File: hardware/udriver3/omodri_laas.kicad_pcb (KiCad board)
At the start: 2 copper layers, 50 x 50 mm, 257 parts, among them J1 Conn_01x11, J10 Conn_01x07, J11 Conn_01x03, J12 Conn_01x03, J13 Conn_01x02, J2 Conn_01x05, J3 Conn_01x03, J4 Conn_01x03, J5 Conn_01x05, J6 Conn_01x05, J7 Conn_01x02, J8 Conn_01x07, J9 Conn_02x04_Odd_Even, Q1 CSD88599Q5DC, Q2 CSD88599Q5DC, Q3 CSD88599Q5DC, Q4 CSD88599Q5DC, Q5 CSD88599Q5DC, Q6 CSD88599Q5DC, SW1 B3U-3100P, U1 TMS320F28388D, U10 DSLVDS1048, U11 TPS3703, U12 TPS3703, U13 TPD6E05U06, U14 DSLVDS1047, U15 TPD2E001, U16 TPD2E001, U17 TPD2E001, U18 TPD2E001, U19 DRV8353S, U2 MAX17502FxTB, U20 DRV8353S, U3 MPM3804GG, U4 MPM3804GG, U5 REF6230, U6 OPA388, U7 TXB0106, U8 TCAN332G, U9 TPD6E05U06, X1 ECS-TXO-2016-33-200-TR

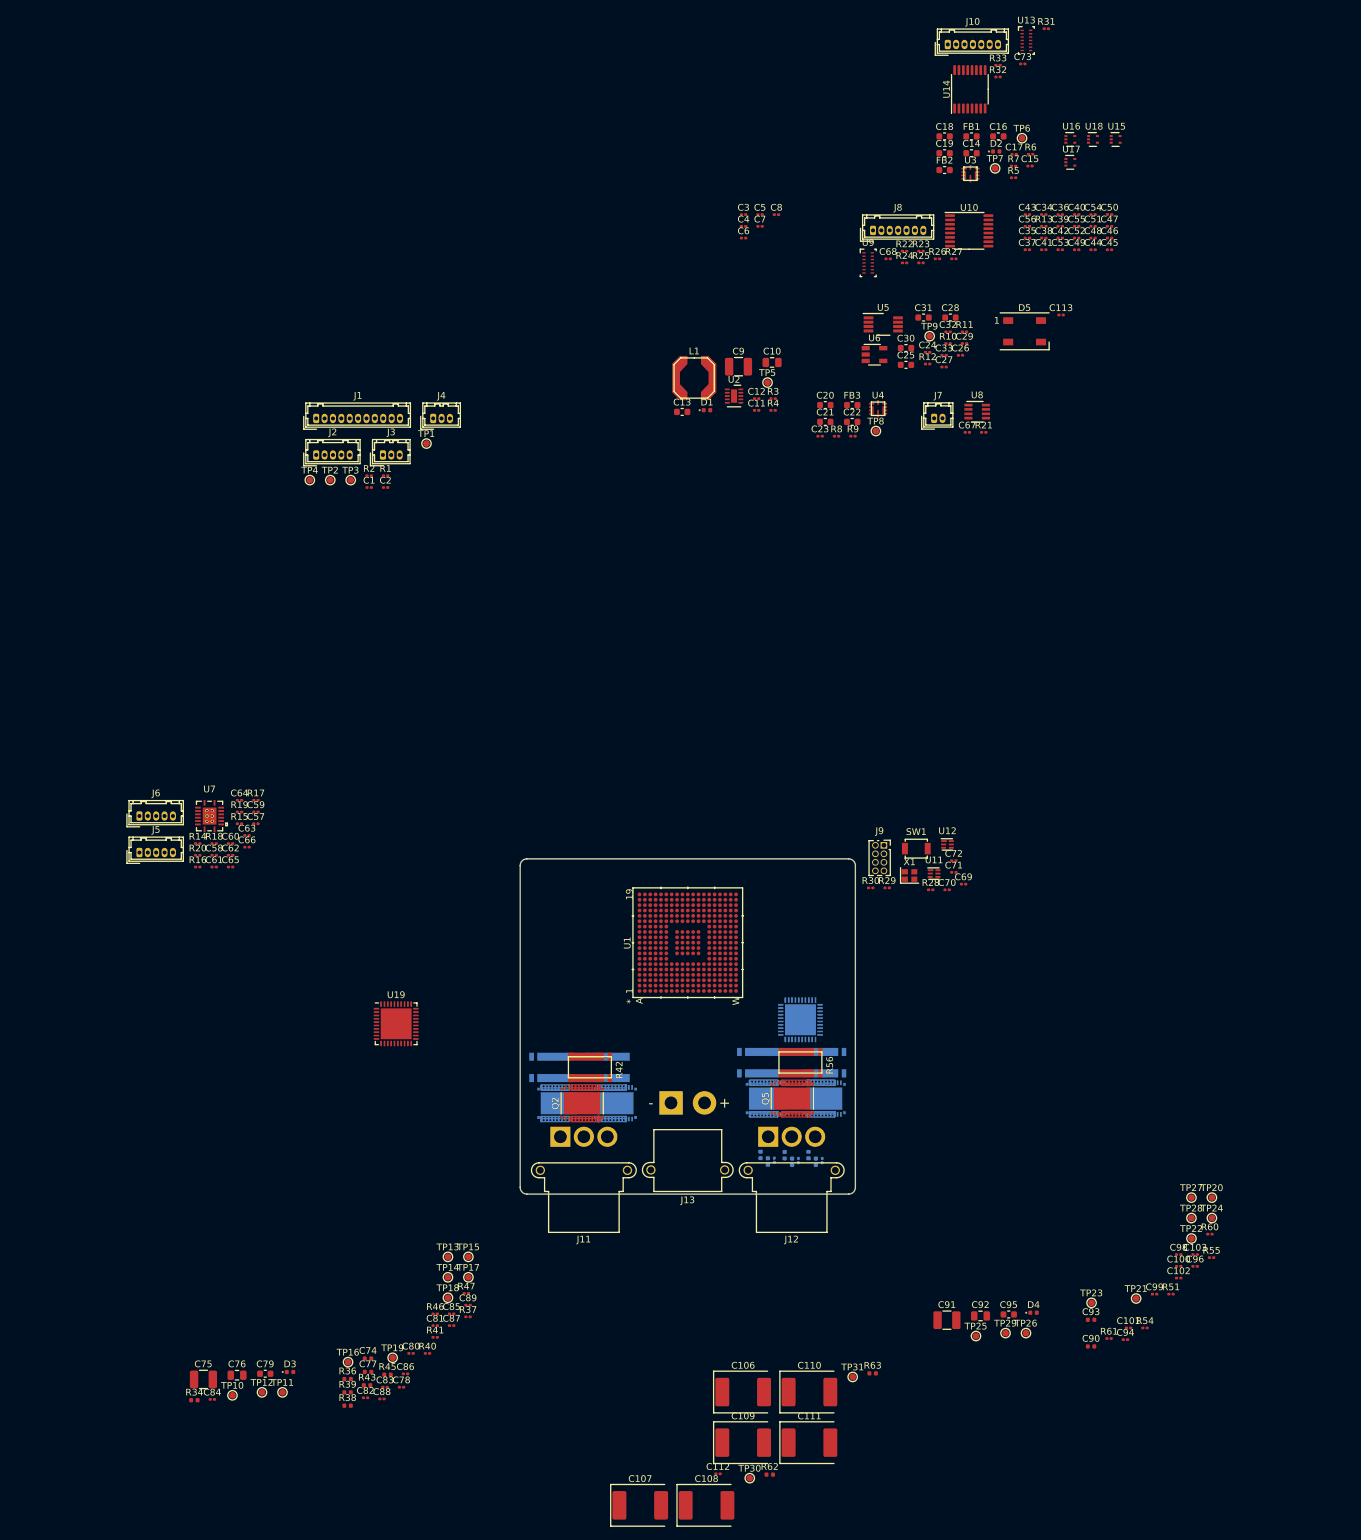
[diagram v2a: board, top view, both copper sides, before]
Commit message: Update of the schematics. Switches on GPIO72 & GPIO84 are missing. J1, J2 & J14 must be merged and connector placement optimized. TCXO must be changed from 20MHz to 25MHz for EtherCAT compatibility. PCB is partially routed in 6-Layers (mainly power supplies and and transistors). 8-Layers will be necessary.
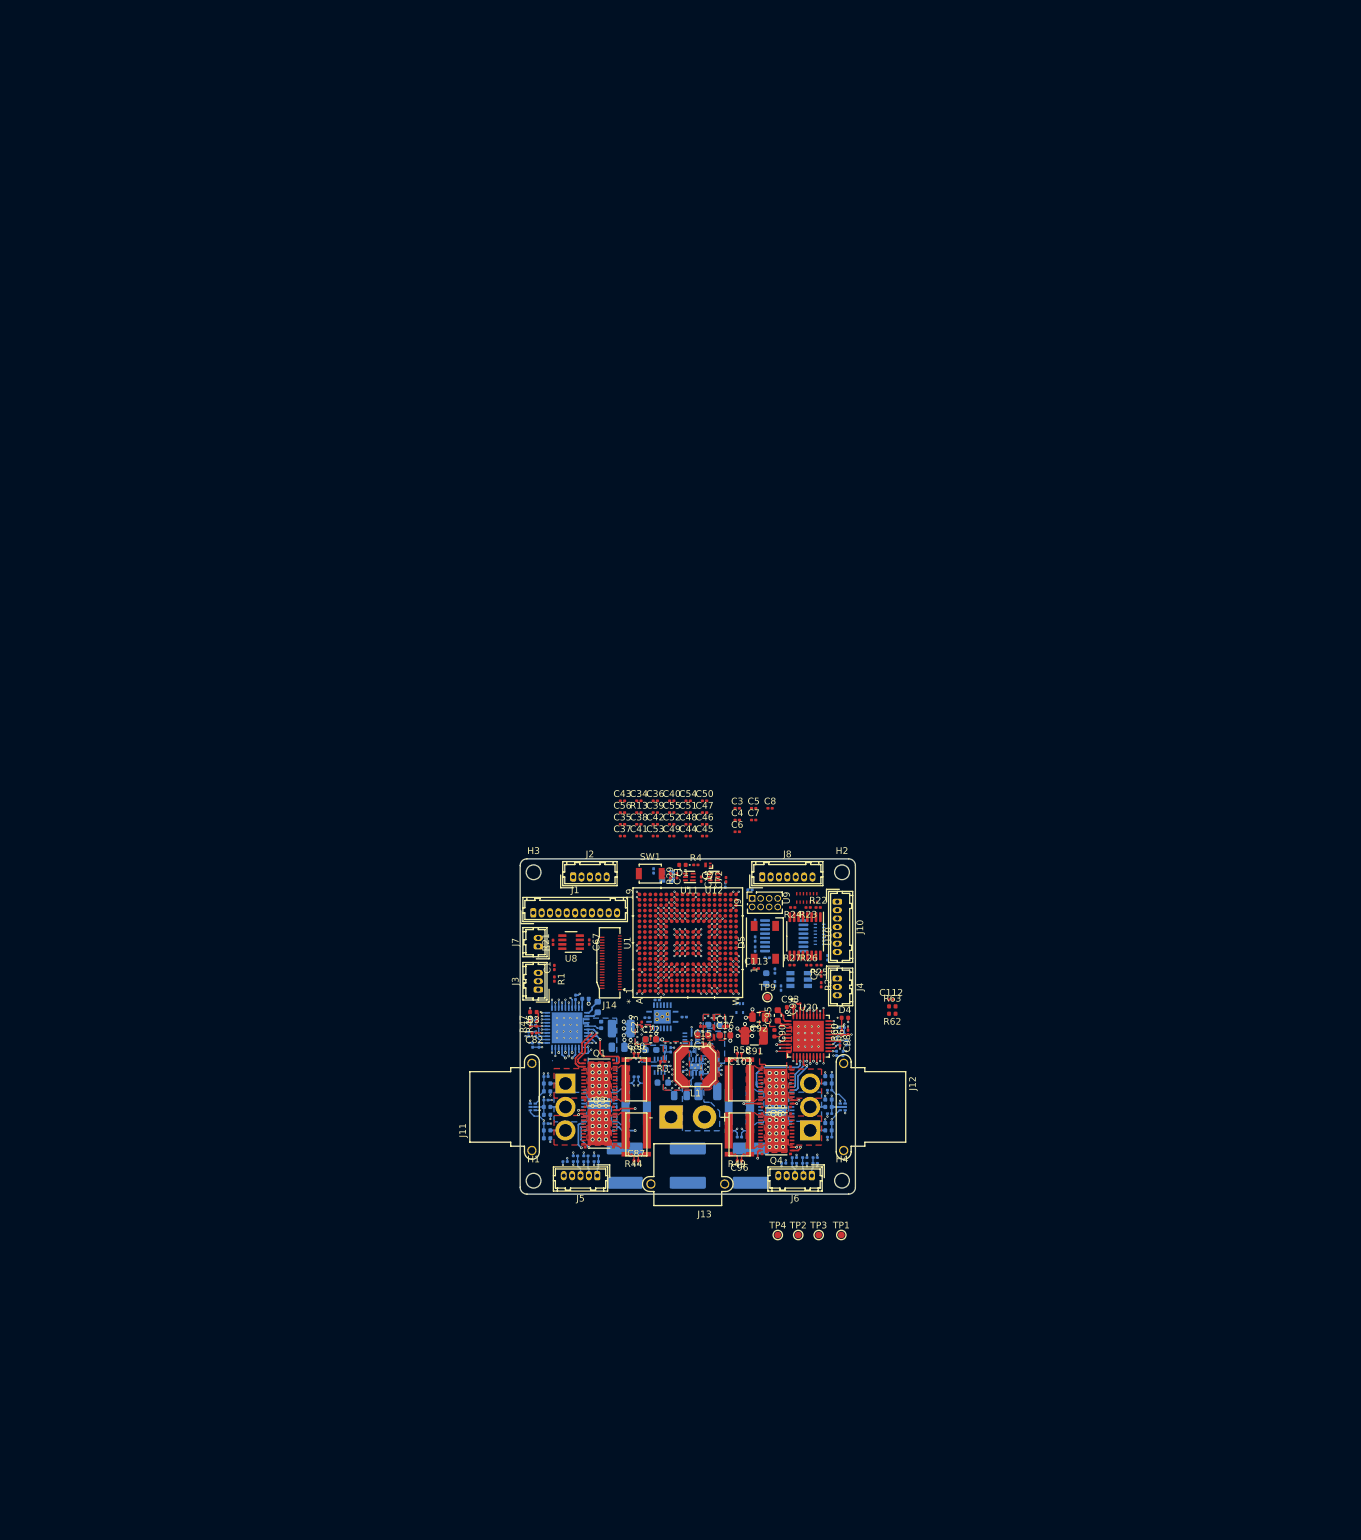
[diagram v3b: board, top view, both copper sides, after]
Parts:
- removed C106, C107, C108, C109, C110, C111: 100uF, Capacitor_Tantalum_SMD:CP_EIA-7360-38_Kemet-E
- removed C20, C25, C30, C31: 10uF, Capacitor_SMD:C_0603_1608Metric
- removed C24, C32, C33, C70: 100nF, Capacitor_SMD:C_0201_0603Metric
- removed D2: LED GREEN, LED_SMD:LED_0402_1005Metric
- removed R10, R11, R12: 0.1, Resistor_SMD:R_0201_0603Metric
- removed R7: 470, Resistor_SMD:R_0201_0603Metric
- removed TP10, TP11, TP12, TP13, TP14, TP15, TP16, TP17, TP18, TP19, TP20, TP21, TP22, TP23, TP24, TP25, TP26, TP27, TP28, TP29, TP30, TP31, TP5, TP6, TP7, TP8: TestPoint, TestPoint:TestPoint_Pad_D1.0mm
- removed U17, U18: TPD2E001, Package_SO:Texas_R-PDSO-N5
- added C114: 22uF, Capacitor_SMD:C_2220_5650Metric, B.Cu at (115.6, 95.8)
- added C115: 22uF, Capacitor_SMD:C_2220_5650Metric, B.Cu at (125.0, 95.8)
- added C116: 22uF, Capacitor_SMD:C_2220_5650Metric, B.Cu at (134.4, 95.8)
- added H1: MountingHole, MountingHole:MountingHole_2.2mm_M2, F.Cu at (102.0, 98.0)
- added H2: MountingHole, MountingHole:MountingHole_2.2mm_M2, F.Cu at (148.0, 52.0)
- added H3: MountingHole, MountingHole:MountingHole_2.2mm_M2, F.Cu at (102.0, 52.0)
- added H4: MountingHole, MountingHole:MountingHole_2.2mm_M2, F.Cu at (148.0, 98.0)
- added J14: Conn_01x40, Connector_FFC-FPC:JAE_FF0841SA1_2Rows-41Pins_P0.40mm_Horizontal, F.Cu at (113.5, 65.5)
- added Q7: NX7002BKM, Package_DFN_QFN:Diodes_DFN1006-3, F.Cu at (128.0, 50.9)
- C10, C100, C101, C102, C11, C12, C13, C26, C27, C28, C29, C57, C58, C59, C60, C61, C62, C63, C64, C65, C66, C68, C69, C73, C74, C75, C76, C77, C78, C79, C81, C83, C84, C85, C86, C88, C89, C9, C99, FB1, FB2, FB3, Q2, Q5, R14, R15, R16, R17, R18, R19, R20, R28, R30, R31, R32, R33, R34, R36, R37, R38, R39, R40, R41, R42, R43, R45, R5, R51, R54, R55, R56, R6, R8, R9, U13, U14, U15, U19, U2, U3, U4, U7, X1: moved to B.Cu
- C18: value 10uF -> 100nF; footprint Capacitor_SMD:C_0603_1608Metric -> Capacitor_SMD:C_0201_0603Metric
- C19, C21: value 22uF -> 10uF; moved to B.Cu
- J11, J12: footprint Connector_AMASS:AMASS_MR30PW-FB_1x03_P3.50mm_Horizontal -> udriver3:AMASS_MR30PW-FB_1x03_P3.50mm_Horizontal
- J13: footprint Connector_AMASS:AMASS_XT30PW-M_1x02_P2.50mm_Horizontal -> udriver3:AMASS_XT30PW-M_1x02_P2.50mm_Horizontal
- Q1, Q3, Q4, Q6, R35, R44, R49, R58, U20: moved to F.Cu
- R4: value 1k -> 470
- U16: value TPD2E001 -> TPD3E001; footprint Package_SO:Texas_R-PDSO-N5 -> udriver3:USON_6; moved to B.Cu
- U5: value REF6230 -> LT6654AIS6-3; footprint Package_SO:VSSOP-8_3.0x3.0mm_P0.65mm -> Package_TO_SOT_SMD:TSOT-23-6; moved to B.Cu
- U6: value OPA388 -> TPD3E001; footprint Package_TO_SOT_SMD:TSOT-23-5 -> udriver3:USON_6; moved to B.Cu
- moved U16 165.1 mm to (101.9, 87.0)
- moved R31 144.0 mm to (135.1, 63.5), turned to 90 degrees
- moved R6 141.7 mm to (127.7, 78.0), turned to 270 degrees
- moved U15 141.2 mm to (132.8, 72.2), turned to 270 degrees
- moved C19 140.2 mm to (129.3, 80.7), turned to 270 degrees
- moved C16 140.2 mm to (130.6, 76.3)
- moved FB1 138.9 mm to (128.1, 75.5), turned to 270 degrees
- moved C73 138.7 mm to (136.8, 64.8)
- moved C14 137.5 mm to (127.2, 76.3), turned to 180 degrees
- moved C15 137.3 mm to (127.2, 75.0), turned to 180 degrees
- moved R5 137.2 mm to (128.6, 78.0), turned to 90 degrees
- moved C17 137.0 mm to (130.6, 75.0)
- moved U13 136.8 mm to (144.7, 61.2)
- moved U3 135.5 mm to (125.6, 76.7)
- moved R32 133.6 mm to (135.1, 62.0), turned to 270 degrees
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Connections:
- net /Power distribution/Sheet5F5BD907/PG_5V0 renamed /Power distribution/OMODRI_Alim_1V2/PG_5V0
- net /Power distribution/Sheet5F5BE68A/3V3 renamed /Power distribution/OMODRI_Alim_3V3/3V3
- net /Power distribution/Sheet5F5BE68A/FB_3V3 renamed /Power distribution/OMODRI_Alim_3V3/FB_3V3
- net /Power distribution/Sheet5F5BF411/1V2 renamed /Power distribution/OMODRI_Alim_1V2/1V2
- net /Power distribution/Sheet5F5BF411/FB_1V2 renamed /Power distribution/OMODRI_Alim_1V2/FB_1V2
- net /Sheet5F71C5AE/DVDD renamed /OMODRI_driver_M1/DVDD
- net /Sheet5F71C5AE/GHA renamed /OMODRI_driver_M1/GHA
- net /Sheet5F71C5AE/GHB renamed /OMODRI_driver_M1/GHB
- net /Sheet5F71C5AE/GHC renamed /OMODRI_driver_M1/GHC
- net /Sheet5F71C5AE/GLA renamed /OMODRI_driver_M1/GLA
- net /Sheet5F71C5AE/GLB renamed /OMODRI_driver_M1/GLB
- net /Sheet5F71C5AE/GLC renamed /OMODRI_driver_M1/GLC
- net /Sheet5F71C5AE/INHA renamed /OMODRI_driver_M1/INHA
- net /Sheet5F71C5AE/INHB renamed /OMODRI_driver_M1/INHB
- net /Sheet5F71C5AE/INHC renamed /OMODRI_driver_M1/INHC
- net /Sheet5F71C5AE/INLA renamed /OMODRI_driver_M1/INLA
- net /Sheet5F71C5AE/INLB renamed /OMODRI_driver_M1/INLB
- net /Sheet5F71C5AE/INLC renamed /OMODRI_driver_M1/INLC
- net /Sheet5F71C5AE/MOTOR_CH1 renamed /OMODRI_driver_M1/MOTOR_CH1
- net /Sheet5F71C5AE/MOTOR_CH2 renamed /OMODRI_driver_M1/MOTOR_CH2
- net /Sheet5F71C5AE/MOTOR_CH3 renamed /OMODRI_driver_M1/MOTOR_CH3
- net /Sheet5F71C5AE/SHA renamed /OMODRI_driver_M1/SHA
- net /Sheet5F71C5AE/SHB renamed /OMODRI_driver_M1/SHB
- net /Sheet5F71C5AE/SHC renamed /OMODRI_driver_M1/SHC
- net /Sheet5F71C5AE/SNB renamed /OMODRI_driver_M1/SNB
- net /Sheet5F71C5AE/SNC renamed /OMODRI_driver_M1/SNC
- net /Sheet5F71C5AE/SPB renamed /OMODRI_driver_M1/SPB
- net /Sheet5F71C5AE/SPC renamed /OMODRI_driver_M1/SPC
- net /Sheet5F71C5AE/VGLS renamed /OMODRI_driver_M1/VGLS
- net /Sheet5F71C92D/DVDD renamed /OMODRI_driver_M2/DVDD
- net /Sheet5F71C92D/GHB renamed /OMODRI_driver_M2/GHB
- net /Sheet5F71C92D/GLB renamed /OMODRI_driver_M2/GLB
- net /Sheet5F71C92D/INHA renamed /OMODRI_driver_M2/INHA
- net /Sheet5F71C92D/INHB renamed /OMODRI_driver_M2/INHB
- net /Sheet5F71C92D/INHC renamed /OMODRI_driver_M2/INHC
- net /Sheet5F71C92D/INLA renamed /OMODRI_driver_M2/INLA
- net /Sheet5F71C92D/INLB renamed /OMODRI_driver_M2/INLB
- net /Sheet5F71C92D/INLC renamed /OMODRI_driver_M2/INLC
- net /Sheet5F71C92D/MOTOR_CH1 renamed /OMODRI_driver_M2/MOTOR_CH1
- net /Sheet5F71C92D/MOTOR_CH2 renamed /OMODRI_driver_M2/MOTOR_CH2
- net /Sheet5F71C92D/MOTOR_CH3 renamed /OMODRI_driver_M2/MOTOR_CH3
- net /Sheet5F71C92D/SHB renamed /OMODRI_driver_M2/SHB
- net /Sheet5F71C92D/SNB renamed /OMODRI_driver_M2/SNB
- net /Sheet5F71C92D/SPB renamed /OMODRI_driver_M2/SPB
- net /Sheet5F71C92D/VGLS renamed /OMODRI_driver_M2/VGLS
- net /Sheet5F9FCB8B/WS2812B_CMD renamed /OMODRI_GPIO/WS2812B_CMD
- net /sheet5F597565/ANALOG_IN1 renamed /OMODRI_GPIO/ANALOG_IN1
- net /sheet5F597565/ANALOG_IN2 renamed /OMODRI_GPIO/ANALOG_IN2
- net /sheet5F597565/COM_SPI_SIMO renamed /OMODRI_GPIO/COM_SPI_SIMO
- net /sheet5F597565/DRV1_GPIO_EN renamed /OMODRI_GPIO/DRV1_GPIO_EN
- net /sheet5F597565/DRV2_GPIO_EN renamed /OMODRI_GPIO/DRV2_GPIO_EN
- net /sheet5F597565/DRV_SPI_CLK renamed /OMODRI_GPIO/DRV_SPI_CLK
- net /sheet5F597565/DRV_SPI_SIMO renamed /OMODRI_GPIO/DRV_SPI_SIMO
- net /sheet5F597565/DRV_SPI_SOMI renamed /OMODRI_GPIO/DRV_SPI_SOMI
- net /sheet5F597565/ENC1_CHA renamed /OMODRI_GPIO/ENC1_CHA
- net /sheet5F597565/ENC1_CHB renamed /OMODRI_GPIO/ENC1_CHB
- net /sheet5F597565/ENC1_CHI renamed /OMODRI_GPIO/ENC1_CHI
- net /sheet5F597565/ENC2_CHB renamed /OMODRI_GPIO/ENC2_CHB
- net /sheet5F597565/FSI_TXA_D0 renamed /OMODRI_GPIO/FSI_TXA_D0
- net /sheet5F597565/FSI_TXA_D1 renamed /OMODRI_GPIO/FSI_TXA_D1
- net /sheet5F597565/GPIO2 renamed /OMODRI_GPIO/GPIO2
- net /sheet5F597565/M1_Ia renamed /OMODRI_GPIO/M1_Ia
- net /sheet5F597565/M1_Ib renamed /OMODRI_GPIO/M1_Ib
- net /sheet5F597565/M1_Ic renamed /OMODRI_GPIO/M1_Ic
- net /sheet5F597565/M1_Vbus renamed /OMODRI_GPIO/M1_Vbus
- net /sheet5F597565/M2_Ia renamed /OMODRI_GPIO/M2_Ia
- net /sheet5F597565/M2_Ib renamed /OMODRI_GPIO/M2_Ib
- net /sheet5F597565/M2_Ic renamed /OMODRI_GPIO/M2_Ic
- net /sheet5F597565/SPI_SIMO renamed /OMODRI_GPIO/SPI_SIMO
- net /sheet5F597565/~DRV1_GPIO_CSn~ renamed /OMODRI_GPIO/~DRV1_GPIO_CSn~
- net /sheet5F597565/~DRV1_GPIO_FAULTn~ renamed /OMODRI_GPIO/~DRV1_GPIO_FAULTn~
- net /sheet5F597565/~DRV2_GPIO_CSn~ renamed /OMODRI_GPIO/~DRV2_GPIO_CSn~
- net /sheet5F597565/~DRV2_GPIO_FAULTn~ renamed /OMODRI_GPIO/~DRV2_GPIO_FAULTn~
- net /sheet5F5A100E/ENC1_A renamed /OMODRI_QuadEncod/ENC1_A
- net /sheet5F5A100E/ENC1_B renamed /OMODRI_QuadEncod/ENC1_B
- net /sheet5F5A100E/ENC1_I renamed /OMODRI_QuadEncod/ENC1_I
- net /sheet5F5A100E/ENC2_B renamed /OMODRI_QuadEncod/ENC2_B
- net /sheet5F5B5755/CAN_H renamed /OMODRI_CAN/CAN_H
- net /sheet5F5B5755/CAN_L renamed /OMODRI_CAN/CAN_L
- net /sheet5F5DA2E4/TX_D0_LVDS_N renamed /OMODRI_FSI_TX/TX_D0_LVDS_N
- net /sheet5F5DA2E4/TX_D0_LVDS_P renamed /OMODRI_FSI_TX/TX_D0_LVDS_P
- C103 pad 1: /Sheet5F71C92D/SPC -> /OMODRI_driver_M2/SPC
- C103 pad 2: /Sheet5F71C92D/SNC -> /OMODRI_driver_M2/SNC
- C104 pad 1: /sheet5F597565/M2_Vb -> /OMODRI_GPIO/M2_Vb
- C105 pad 1: /sheet5F597565/M2_Vc -> /OMODRI_GPIO/M2_Vc
- C18 pad 1: 5V0 -> VDD_3V3
- C27 pad 1: Net-(C27-Pad1) -> VDDA_3V3
- C28 pad 1: Net-(C28-Pad1) -> REF_3V0_BUF
- C29 pad 1: /Power distribution/Sheet5F5C0182/REF_3V0 -> REF_3V0_BUF
- C63 pad 1: /sheet5F5A100E/ENC2_A -> /OMODRI_QuadEncod/ENC2_A
- C65 pad 1: /sheet5F5A100E/ENC2_I -> /OMODRI_QuadEncod/ENC2_I
- C80 pad 1: /Sheet5F71C5AE/SPA -> /OMODRI_driver_M1/SPA
- C80 pad 2: /Sheet5F71C5AE/SNA -> /OMODRI_driver_M1/SNA
- C81 pad 1: /sheet5F597565/M1_Va -> /OMODRI_GPIO/M1_Va
- C88 pad 1: /sheet5F597565/M1_Vb -> /OMODRI_GPIO/M1_Vb
- C89 pad 1: /sheet5F597565/M1_Vc -> /OMODRI_GPIO/M1_Vc
- C96 pad 1: /Sheet5F71C92D/SPA -> /OMODRI_driver_M2/SPA
- C96 pad 2: /Sheet5F71C92D/SNA -> /OMODRI_driver_M2/SNA
- C97 pad 1: /sheet5F597565/M2_Va -> /OMODRI_GPIO/M2_Va
- D1 pad 2: 5V0 -> VDD_3V3
- J1 pad 10: /sheet5F597565/GPIO3 -> /OMODRI_GPIO/GPIO1
- J1 pad 11: /sheet5F597565/GPIO4 -> /OMODRI_GPIO/GPIO0
- J1 pad 3: /sheet5F597565/COM_SPI_SOMI -> /OMODRI_GPIO/~COM_SPI_CSn~
- J1 pad 4: /sheet5F597565/COM_SPI_CLK -> /OMODRI_GPIO/COM_SPI_SOMI
- J1 pad 5: /sheet5F597565/~COM_SPI_CSn~ -> /OMODRI_GPIO/COM_SPI_CLK
- J1 pad 7: /sheet5F597565/GPIO0 -> /OMODRI_GPIO/GPIO4
- J1 pad 8: /sheet5F597565/GPIO1 -> /OMODRI_GPIO/GPIO3
- J10 pad 2: /sheet5F5DA2E4/TX_CLK_LVDS_N -> /OMODRI_FSI_TX/TX_CLK_LVDS_N
- J10 pad 3: /sheet5F5DA2E4/TX_CLK_LVDS_P -> /OMODRI_FSI_TX/TX_CLK_LVDS_P
- J10 pad 6: /sheet5F5DA2E4/TX_D1_LVDS_N -> /OMODRI_FSI_TX/TX_D1_LVDS_P
- J10 pad 7: /sheet5F5DA2E4/TX_D1_LVDS_P -> /OMODRI_FSI_TX/TX_D1_LVDS_N
- J13 pad 1: VPOWER -> GND
- J13 pad 2: GND -> VPOWER
- J2 pad 2: /sheet5F597565/SPI_SOMI -> /OMODRI_GPIO/~SPI_CSn~
- J2 pad 3: /sheet5F597565/SPI_CLK -> /OMODRI_GPIO/SPI_SOMI
- J2 pad 4: /sheet5F597565/~SPI_CSn~ -> /OMODRI_GPIO/SPI_CLK
- J6 pad 1: /sheet5F5A100E/ENC2_A -> /OMODRI_QuadEncod/ENC2_A
- J6 pad 3: /sheet5F5A100E/ENC2_I -> /OMODRI_QuadEncod/ENC2_I
- J8 pad 2: /sheet5F5B5756/RX_CLK_LVDS_N -> /OMODRI_FSI_RX/RX_CLK_LVDS_N
- J8 pad 3: /sheet5F5B5756/RX_CLK_LVDS_P -> /OMODRI_FSI_RX/RX_CLK_LVDS_P
- J8 pad 4: /sheet5F5B5756/RX_D0_LVDS_N -> /OMODRI_FSI_RX/RX_D0_LVDS_N
- J8 pad 5: /sheet5F5B5756/RX_D0_LVDS_P -> /OMODRI_FSI_RX/RX_D0_LVDS_P
- J8 pad 6: /sheet5F5B5756/RX_D1_LVDS_N -> /OMODRI_FSI_RX/RX_D1_LVDS_P
- J8 pad 7: /sheet5F5B5756/RX_D1_LVDS_P -> /OMODRI_FSI_RX/RX_D1_LVDS_N
- Q4 pad 1: /Sheet5F71C92D/GHA -> /OMODRI_driver_M2/GHA
- Q4 pad 2: /Sheet5F71C92D/SHA -> /OMODRI_driver_M2/SHA
- Q4 pad 22: /Sheet5F71C92D/GLA -> /OMODRI_driver_M2/GLA
- Q6 pad 1: /Sheet5F71C92D/GHC -> /OMODRI_driver_M2/GHC
- Q6 pad 2: /Sheet5F71C92D/SHC -> /OMODRI_driver_M2/SHC
- Q6 pad 22: /Sheet5F71C92D/GLC -> /OMODRI_driver_M2/GLC
- R17 pad 2: /sheet5F5A100E/ENC2_A -> /OMODRI_QuadEncod/ENC2_A
- R19 pad 2: /sheet5F5A100E/ENC2_I -> /OMODRI_QuadEncod/ENC2_I
- R22 pad 1: /sheet5F5B5756/RX_CLK_LVDS_P -> /OMODRI_FSI_RX/RX_D1_LVDS_P
- R22 pad 2: /sheet5F5B5756/RX_CLK_LVDS_N -> /OMODRI_FSI_RX/RX_D1_LVDS_N
- R23 pad 1: /sheet5F5B5756/RX_D0_LVDS_P -> /OMODRI_FSI_RX/RX_D0_LVDS_P
- R23 pad 2: /sheet5F5B5756/RX_D0_LVDS_N -> /OMODRI_FSI_RX/RX_D0_LVDS_N
- R24 pad 1: /sheet5F5B5756/RX_D1_LVDS_P -> /OMODRI_FSI_RX/RX_CLK_LVDS_P
- R24 pad 2: /sheet5F5B5756/RX_D1_LVDS_N -> /OMODRI_FSI_RX/RX_CLK_LVDS_N
- R25 pad 2: /sheet5F597565/FSI_RXA_CLK -> /OMODRI_GPIO/FSI_RXC_D1
- R26 pad 2: /sheet5F597565/FSI_RXA_D0 -> /OMODRI_GPIO/FSI_RXC_D0
- R27 pad 2: /sheet5F597565/FSI_RXA_D1 -> /OMODRI_GPIO/FSI_RXC_CLK
- R33 pad 2: /sheet5F597565/FSI_TXA_CLK -> /OMODRI_GPIO/FSI_TXA_CLK
- R34 pad 2: /sheet5F597565/M1_Va -> /OMODRI_GPIO/M1_Va
- R35 pad 1: GND -> Net-(Q1-Pad12)
- R35 pad 2: /Sheet5F71C5AE/SNA -> /OMODRI_driver_M1/SPA
- R35 pad 3: /Sheet5F71C5AE/SPA -> /OMODRI_driver_M1/SNA
- R35 pad 4: Net-(Q1-Pad12) -> GND
- R36 pad 1: /sheet5F597565/M1_Va -> /OMODRI_GPIO/M1_Va
- R38 pad 2: /sheet5F597565/M1_Vb -> /OMODRI_GPIO/M1_Vb
- R39 pad 2: /sheet5F597565/M1_Vc -> /OMODRI_GPIO/M1_Vc
- R4 pad 2: GND -> Net-(Q7-Pad3)
- R43 pad 1: /sheet5F597565/M1_Vb -> /OMODRI_GPIO/M1_Vb
- R45 pad 1: /sheet5F597565/M1_Vc -> /OMODRI_GPIO/M1_Vc
- R48 pad 2: /sheet5F597565/M2_Va -> /OMODRI_GPIO/M2_Va
- R49 pad 1: GND -> Net-(Q4-Pad12)
- R49 pad 2: /Sheet5F71C92D/SNA -> /OMODRI_driver_M2/SPA
- R49 pad 3: /Sheet5F71C92D/SPA -> /OMODRI_driver_M2/SNA
- R49 pad 4: Net-(Q4-Pad12) -> GND
- R50 pad 1: /sheet5F597565/M2_Va -> /OMODRI_GPIO/M2_Va
- R52 pad 2: /sheet5F597565/M2_Vb -> /OMODRI_GPIO/M2_Vb
- R53 pad 2: /sheet5F597565/M2_Vc -> /OMODRI_GPIO/M2_Vc
- R57 pad 1: /sheet5F597565/M2_Vb -> /OMODRI_GPIO/M2_Vb
- R58 pad 1: Net-(Q6-Pad12) -> GND
- R58 pad 2: /Sheet5F71C92D/SPC -> /OMODRI_driver_M2/SNC
- R58 pad 3: /Sheet5F71C92D/SNC -> /OMODRI_driver_M2/SPC
- R58 pad 4: GND -> Net-(Q6-Pad12)
- R59 pad 1: /sheet5F597565/M2_Vc -> /OMODRI_GPIO/M2_Vc
- U1 pad A12: Net-(U1-PadA12) -> /OMODRI_GPIO/ESC_MDIO_DATA
- U1 pad A13: Net-(U1-PadA13) -> /OMODRI_GPIO/ESC_PHY1_LINKSTATUS
- U1 pad A14: /sheet5F597565/GPIO4 -> /OMODRI_GPIO/GPIO4
- U1 pad A16: /sheet5F597565/GPIO0 -> /OMODRI_GPIO/GPIO0
- U1 pad A17: /sheet5F597565/SPI_SOMI -> /OMODRI_GPIO/SPI_SOMI
- U1 pad A8: Net-(U1-PadA8) -> /OMODRI_GPIO/ESC_RX0_CLK
- U1 pad B10: Net-(U1-PadB10) -> /OMODRI_GPIO/ESC_TX0_CLK
- U1 pad B12: Net-(U1-PadB12) -> /OMODRI_GPIO/ECAT0_INT
- U1 pad B13: Net-(U1-PadB13) -> /OMODRI_GPIO/ESC_I2C_SDA
- U1 pad B14: /sheet5F597565/GPIO3 -> /OMODRI_GPIO/GPIO3
- U1 pad B15: /sheet5F597565/GPIO1 -> /OMODRI_GPIO/GPIO1
- U1 pad B16: /sheet5F597565/~SPI_CSn~ -> /OMODRI_GPIO/~SPI_CSn~
- U1 pad B17: /sheet5F597565/SPI_CLK -> /OMODRI_GPIO/SPI_CLK
- U1 pad B8: Net-(U1-PadB8) -> /OMODRI_GPIO/ESC_RX0_ERR
- U1 pad B9: Net-(U1-PadB9) -> /OMODRI_GPIO/ESC_TX0_D2
- U1 pad C10: Net-(U1-PadC10) -> /OMODRI_GPIO/ESC_TX0_D0
- U1 pad C12: Net-(U1-PadC12) -> /OMODRI_GPIO/~ESC_PHY_RESETn~
- U1 pad C13: Net-(U1-PadC13) -> /OMODRI_GPIO/ESC_I2C_SCL
- U1 pad C2: Net-(U1-PadC2) -> /OMODRI_GPIO/CAN_TX
- U1 pad C4: Net-(U1-PadC4) -> /OMODRI_GPIO/ESC_RX0_D2
- U1 pad C5: Net-(U1-PadC5) -> /OMODRI_GPIO/ESC_RX0_D0
- U1 pad C9: Net-(U1-PadC9) -> /OMODRI_GPIO/ESC_TX0_D3
- U1 pad D1: Net-(U1-PadD1) -> /OMODRI_GPIO/CAN_RX
- U1 pad D10: Net-(U1-PadD10) -> /OMODRI_GPIO/ESC_TX0_D1
- U1 pad D12: Net-(U1-PadD12) -> /OMODRI_GPIO/ESC_TX0_ENA
- U1 pad D13: Net-(U1-PadD13) -> /OMODRI_GPIO/ESC_MDIO_CLK
- U1 pad D14: Net-(U1-PadD14) -> /OMODRI_GPIO/ESC_PHY0_LINKSTATUS
- U1 pad D18: Net-(U1-PadD18) -> /OMODRI_GPIO/ESC_LED_RUN
- U1 pad D4: Net-(U1-PadD4) -> /OMODRI_GPIO/ESC_RX0_D3
- U1 pad D5: Net-(U1-PadD5) -> /OMODRI_GPIO/ESC_RX0_D1
- U1 pad D9: Net-(U1-PadD9) -> /OMODRI_GPIO/ESC_RX0_DV
- U1 pad E17: Net-(U1-PadE17) -> /OMODRI_GPIO/ESC_LED_ERR
- U1 pad F17: Net-(U1-PadF17) -> /OMODRI_GPIO/ESC_LED_LINK1_ACTIVE
- U1 pad F18: Net-(U1-PadF18) -> /OMODRI_GPIO/ESC_LED_LINK0_ACTIVE
- U1 pad J16: /sheet5F597565/CAN_TX -> Net-(U1-PadJ16)
- U1 pad J17: /sheet5F597565/CAN_RX -> Net-(U1-PadJ17)
- U1 pad K1: /sheet5F597565/ENC2_CHI -> /OMODRI_GPIO/ENC2_CHI
- U1 pad K16: /sheet5F597565/COM_SPI_CLK -> /OMODRI_GPIO/COM_SPI_CLK
- U1 pad K3: /sheet5F597565/ENC2_CHA -> /OMODRI_GPIO/ENC2_CHA
- U1 pad L16: /sheet5F597565/COM_SPI_SOMI -> /OMODRI_GPIO/COM_SPI_SOMI
- U1 pad L19: Net-(U1-PadL19) -> /OMODRI_GPIO/ESC_RX1_D3
- U1 pad M16: /sheet5F597565/~COM_SPI_CSn~ -> /OMODRI_GPIO/~COM_SPI_CSn~
- U1 pad M18: Net-(U1-PadM18) -> /OMODRI_GPIO/ESC_RX1_D2
- U1 pad M19: Net-(U1-PadM19) -> /OMODRI_GPIO/ESC_RX1_D1
- U1 pad N19: Net-(U1-PadN19) -> /OMODRI_GPIO/ESC_RX1_D0
- U1 pad P16: /sheet5F597565/FSI_RXA_D0 -> Net-(U1-PadP16)
- U1 pad P17: /sheet5F597565/FSI_RXA_D1 -> Net-(U1-PadP17)
- U1 pad P18: /sheet5F597565/FSI_RXA_CLK -> Net-(U1-PadP18)
- U1 pad R19: /sheet5F597565/FSI_TXA_CLK -> /OMODRI_GPIO/FSI_TXA_CLK
- U1 pad T10: Net-(U1-PadT10) -> /OMODRI_GPIO/ESC_TX1_ENA
- U1 pad T17: Net-(U1-PadT17) -> /OMODRI_GPIO/ESC_RX1_DV
- U1 pad T18: Net-(U1-PadT18) -> /OMODRI_GPIO/ESC_RX1_CLK
- U1 pad T19: Net-(U1-PadT19) -> /OMODRI_GPIO/ESC_RX1_ERR
- U1 pad T2: /sheet5F597565/M2_Va -> /OMODRI_GPIO/M2_Va
- U1 pad T6: /sheet5F597565/M1_Vc -> /OMODRI_GPIO/M1_Vc
- U1 pad U10: Net-(U1-PadU10) -> /OMODRI_GPIO/ESC_TX1_CLK
- U1 pad U12: Net-(U1-PadU12) -> /OMODRI_GPIO/FSI_RXC_CLK
- U1 pad U18: Net-(U1-PadU18) -> /OMODRI_GPIO/ESC_TX1_D3
- U1 pad U2: /sheet5F597565/M1_Va -> /OMODRI_GPIO/M1_Va
- U1 pad U6: /sheet5F597565/M2_Vc -> /OMODRI_GPIO/M2_Vc
- U1 pad V10: Net-(U1-PadV10) -> /OMODRI_GPIO/ESC_TX1_D0
- U1 pad V12: Net-(U1-PadV12) -> /OMODRI_GPIO/FSI_RXC_D0
- U1 pad V18: Net-(U1-PadV18) -> /OMODRI_GPIO/ESC_TX1_D2
- U1 pad V3: /sheet5F597565/M1_Vb -> /OMODRI_GPIO/M1_Vb
- U1 pad W10: Net-(U1-PadW10) -> /OMODRI_GPIO/FSI_RXC_D1
- U1 pad W18: Net-(U1-PadW18) -> /OMODRI_GPIO/ESC_TX1_D1
- U1 pad W3: /sheet5F597565/M2_Vb -> /OMODRI_GPIO/M2_Vb
- U1 pad W9: Net-(U1-PadW9) -> /OMODRI_GPIO/ECAT1_INT
- U10 pad 1: /sheet5F5B5756/RX_CLK_LVDS_N -> /OMODRI_FSI_RX/RX_D1_LVDS_N
- U10 pad 10: Net-(U10-Pad10) -> /OMODRI_GPIO/FSI_RXC_CLK
- U10 pad 11: /sheet5F597565/FSI_RXA_D1 -> Net-(U10-Pad11)
- U10 pad 14: /sheet5F597565/FSI_RXA_D0 -> /OMODRI_GPIO/FSI_RXC_D0
- U10 pad 15: /sheet5F597565/FSI_RXA_CLK -> /OMODRI_GPIO/FSI_RXC_D1
- U10 pad 2: /sheet5F5B5756/RX_CLK_LVDS_P -> /OMODRI_FSI_RX/RX_D1_LVDS_P
- U10 pad 3: /sheet5F5B5756/RX_D0_LVDS_P -> /OMODRI_FSI_RX/RX_D0_LVDS_P
- U10 pad 4: /sheet5F5B5756/RX_D0_LVDS_N -> /OMODRI_FSI_RX/RX_D0_LVDS_N
- U10 pad 5: /sheet5F5B5756/RX_D1_LVDS_N -> Net-(U10-Pad5)
- U10 pad 6: /sheet5F5B5756/RX_D1_LVDS_P -> Net-(U10-Pad6)
- U10 pad 7: Net-(U10-Pad7) -> /OMODRI_FSI_RX/RX_CLK_LVDS_P
- U10 pad 8: Net-(U10-Pad8) -> /OMODRI_FSI_RX/RX_CLK_LVDS_N
- U13 pad 1: /sheet5F5DA2E4/TX_CLK_LVDS_N -> /OMODRI_FSI_TX/TX_D1_LVDS_N
- U13 pad 13: /sheet5F5DA2E4/TX_CLK_LVDS_P -> /OMODRI_FSI_TX/TX_D1_LVDS_P
- U13 pad 14: /sheet5F5DA2E4/TX_CLK_LVDS_N -> /OMODRI_FSI_TX/TX_D1_LVDS_N
- U13 pad 2: /sheet5F5DA2E4/TX_CLK_LVDS_P -> /OMODRI_FSI_TX/TX_D1_LVDS_P
- U13 pad 6: /sheet5F5DA2E4/TX_D1_LVDS_N -> /OMODRI_FSI_TX/TX_CLK_LVDS_P
- U13 pad 7: /sheet5F5DA2E4/TX_D1_LVDS_P -> /OMODRI_FSI_TX/TX_CLK_LVDS_N
- U13 pad 8: /sheet5F5DA2E4/TX_D1_LVDS_P -> /OMODRI_FSI_TX/TX_CLK_LVDS_N
- U13 pad 9: /sheet5F5DA2E4/TX_D1_LVDS_N -> /OMODRI_FSI_TX/TX_CLK_LVDS_P
- U14 pad 10: Net-(U14-Pad10) -> /OMODRI_FSI_TX/TX_CLK_LVDS_P
- U14 pad 11: /sheet5F5DA2E4/TX_D1_LVDS_P -> Net-(U14-Pad11)
- U14 pad 12: /sheet5F5DA2E4/TX_D1_LVDS_N -> Net-(U14-Pad12)
- U14 pad 15: /sheet5F5DA2E4/TX_CLK_LVDS_P -> /OMODRI_FSI_TX/TX_D1_LVDS_P
- U14 pad 16: /sheet5F5DA2E4/TX_CLK_LVDS_N -> /OMODRI_FSI_TX/TX_D1_LVDS_N
- U14 pad 6: /sheet5F597565/FSI_TXA_CLK -> Net-(U14-Pad6)
- U14 pad 7: Net-(U14-Pad7) -> /OMODRI_GPIO/FSI_TXA_CLK
- U14 pad 9: Net-(U14-Pad9) -> /OMODRI_FSI_TX/TX_CLK_LVDS_N
- U15 pad 1: VDDA_3V3 -> VDD_3V3
- U16 pad 1: VDDA_3V3 -> /OMODRI_GPIO/M1_Vc
- U16 pad 2: /sheet5F597565/M2_Vb -> /OMODRI_GPIO/M1_Vb
- U16 pad 3: /sheet5F597565/M1_Vb -> GND
- U16 pad 4: GND -> /OMODRI_GPIO/M1_Va
- U16 pad 5: /sheet5F597565/M2_Vb -> /OMODRI_GPIO/M1_Vb
- U19 pad 10: /Sheet5F71C5AE/SNA -> /OMODRI_driver_M1/SNA
- U19 pad 9: /Sheet5F71C5AE/SPA -> /OMODRI_driver_M1/SPA
- U20 pad 10: /Sheet5F71C92D/SNC -> /OMODRI_driver_M2/SNA
- U20 pad 16: /Sheet5F71C92D/GHA -> /OMODRI_driver_M2/GHC
- U20 pad 17: /Sheet5F71C92D/SHA -> /OMODRI_driver_M2/SHC
- U20 pad 18: /Sheet5F71C92D/GLA -> /OMODRI_driver_M2/GLC
- U20 pad 19: /Sheet5F71C92D/SPA -> /OMODRI_driver_M2/SPC
- U20 pad 20: /Sheet5F71C92D/SNA -> /OMODRI_driver_M2/SNC
- U20 pad 6: /Sheet5F71C92D/GHC -> /OMODRI_driver_M2/GHA
- U20 pad 7: /Sheet5F71C92D/SHC -> /OMODRI_driver_M2/SHA
- U20 pad 8: /Sheet5F71C92D/GLC -> /OMODRI_driver_M2/GLA
- U20 pad 9: /Sheet5F71C92D/SPC -> /OMODRI_driver_M2/SPA
- U5 pad 1: VDDA_3V3 -> GND
- U5 pad 2: VDDA_3V3 -> GND
- U5 pad 3: VDDA_3V3 -> Net-(U5-Pad3)
- U5 pad 4: Net-(C27-Pad1) -> VDDA_3V3
- U5 pad 5: /Power distribution/Sheet5F5C0182/REF_3V0 -> Net-(U5-Pad5)
- U5 pad 6: /Power distribution/Sheet5F5C0182/REF_3V0 -> REF_3V0_BUF
- U6 pad 1: REF_3V0_BUF -> /OMODRI_GPIO/M2_Vc
- U6 pad 2: GND -> /OMODRI_GPIO/M2_Vb
- U6 pad 3: /Power distribution/Sheet5F5C0182/REF_3V0 -> GND
- U6 pad 4: REF_3V0_BUF -> /OMODRI_GPIO/M2_Va
- U6 pad 5: VDDA_3V3 -> /OMODRI_GPIO/M2_Vb
- U7 pad 10: /sheet5F5A100E/ENC2_I -> /OMODRI_QuadEncod/ENC2_A
- U7 pad 12: /sheet5F5A100E/ENC2_A -> /OMODRI_QuadEncod/ENC2_I
- U7 pad 5: /sheet5F597565/ENC2_CHA -> /OMODRI_GPIO/ENC2_CHI
- U7 pad 7: /sheet5F597565/ENC2_CHI -> /OMODRI_GPIO/ENC2_CHA
- U8 pad 1: /sheet5F597565/CAN_TX -> /OMODRI_GPIO/CAN_TX
- U8 pad 4: /sheet5F597565/CAN_RX -> /OMODRI_GPIO/CAN_RX
- U9 pad 1: /sheet5F5B5756/RX_CLK_LVDS_N -> /OMODRI_FSI_RX/RX_CLK_LVDS_N
- U9 pad 11: /sheet5F5B5756/RX_D0_LVDS_N -> /OMODRI_FSI_RX/RX_D0_LVDS_P
- U9 pad 12: /sheet5F5B5756/RX_D0_LVDS_P -> /OMODRI_FSI_RX/RX_D0_LVDS_N
- U9 pad 13: /sheet5F5B5756/RX_CLK_LVDS_P -> /OMODRI_FSI_RX/RX_CLK_LVDS_P
- U9 pad 14: /sheet5F5B5756/RX_CLK_LVDS_N -> /OMODRI_FSI_RX/RX_CLK_LVDS_N
- U9 pad 2: /sheet5F5B5756/RX_CLK_LVDS_P -> /OMODRI_FSI_RX/RX_CLK_LVDS_P
- U9 pad 3: /sheet5F5B5756/RX_D0_LVDS_P -> /OMODRI_FSI_RX/RX_D0_LVDS_N
- U9 pad 4: /sheet5F5B5756/RX_D0_LVDS_N -> /OMODRI_FSI_RX/RX_D0_LVDS_P
- U9 pad 6: /sheet5F5B5756/RX_D1_LVDS_N -> /OMODRI_FSI_RX/RX_D1_LVDS_P
- U9 pad 7: /sheet5F5B5756/RX_D1_LVDS_P -> /OMODRI_FSI_RX/RX_D1_LVDS_N
- U9 pad 8: /sheet5F5B5756/RX_D1_LVDS_P -> /OMODRI_FSI_RX/RX_D1_LVDS_N
- U9 pad 9: /sheet5F5B5756/RX_D1_LVDS_N -> /OMODRI_FSI_RX/RX_D1_LVDS_P
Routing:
- net GND: track 0.00 -> 97.4 mm, vias 0 -> 181
- net /OMODRI_GPIO/DRV_SPI_CLK: track 0.00 -> 51.3 mm, vias 0 -> 3
- net /OMODRI_GPIO/DRV_SPI_SOMI: track 0.00 -> 51.0 mm, vias 0 -> 3
- net /OMODRI_GPIO/DRV_SPI_SIMO: track 0.00 -> 49.5 mm, vias 0 -> 4
- net /OMODRI_GPIO/~DRV2_GPIO_FAULTn~: track 0.00 -> 37.1 mm, vias 0 -> 2
- net /OMODRI_driver_M1/GHB: track 0.00 -> 36.5 mm, vias 0 -> 2
- net /OMODRI_driver_M1/SHB: track 0.00 -> 35.1 mm, vias 0 -> 2
- net /OMODRI_driver_M1/SNC: track 0.00 -> 31.9 mm, vias 0 -> 2
- net /OMODRI_driver_M1/SPC: track 0.00 -> 30.3 mm, vias 0 -> 2
- net /OMODRI_GPIO/~DRV2_GPIO_CSn~: track 0.00 -> 29.5 mm, vias 0 -> 2
- net /OMODRI_driver_M2/SPA: track 0.00 -> 28.5 mm, vias 0 -> 2
- net /OMODRI_driver_M2/SNA: track 0.00 -> 28.2 mm, vias 0 -> 2
- net /OMODRI_driver_M2/GLC: track 0.00 -> 27.0 mm, vias 0 -> 2
- net /OMODRI_GPIO/~DRV1_GPIO_FAULTn~: track 0.00 -> 25.8 mm, vias 0 -> 2
- net /OMODRI_driver_M1/GLB: track 0.00 -> 24.3 mm, vias 0 -> 2
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- added copper zone on F.Cu, net /OMODRI_driver_M1/MOTOR_CH1
- added copper zone on B.Cu, net /OMODRI_driver_M1/MOTOR_CH2
- added copper zone on F.Cu, net /OMODRI_driver_M1/MOTOR_CH3
- added copper zone on F.Cu, net /OMODRI_driver_M2/MOTOR_CH1
- added copper zone on B.Cu, net /OMODRI_driver_M2/MOTOR_CH2
- added copper zone on F.Cu, net /OMODRI_driver_M2/MOTOR_CH3
- added copper zone on B.Cu, net /Power distribution/OMODRI_Alim_1V2/1V2
- added copper zone on B.Cu, net /Power distribution/OMODRI_Alim_3V3/3V3
- added copper zone on B.Cu, net 5V0
- added copper zone on F.Cu, net 5V0
- added copper zone on B.Cu, net Net-(L1-Pad1)
- added copper zone on F.Cu, net Net-(L1-Pad1)
- added copper zone on F.Cu, net Net-(Q1-Pad12)
- added copper zone on B.Cu, net Net-(Q2-Pad12)
- added copper zone on F.Cu, net Net-(Q3-Pad12)
- added copper zone on F.Cu, net Net-(Q4-Pad12)
- added copper zone on B.Cu, net Net-(Q5-Pad12)
- added copper zone on F.Cu, net Net-(Q6-Pad12)
- added copper zone on B.Cu, net VDDA_3V3
- added copper zone on F.Cu, net VDDA_3V3
- added copper zone on B.Cu, net VDD_1V2
- added copper zone on F.Cu, net VDD_1V2
- added copper zone on B.Cu, net VDD_3V3
- added copper zone on F.Cu, net VDD_3V3
- added copper zone on B.Cu, net VPOWER
- added copper zone on F.Cu, net VPOWER
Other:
- copper layers 2 -> 6
- net class Default: clearance 0.2 -> 0.127; trace_width 0.25 -> 0.15; via_dia 0.8 -> 0.31; via_drill 0.4 -> 0.15
- net class Power added: clearance 0.15, trace_width 0.25, via_dia 0.4, via_drill 0.2
- net class Power_Plan added: clearance 0.15, trace_width 0.25, via_dia 0.6, via_drill 0.35
- rule trace_clearance: 0.2 -> 0.127
- rule trace_min: 0.2 -> 0.127
- rule via_min_drill: 0.3 -> 0.1
- rule via_min_size: 0.4 -> 0.3032
